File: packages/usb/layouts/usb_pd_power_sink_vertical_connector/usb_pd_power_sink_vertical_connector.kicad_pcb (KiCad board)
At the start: 2 copper layers, 8 parts, among them U2 2.9V

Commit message: WIP update usb
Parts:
- C1: value 1µF ±10% 16V X5R -> 1µF ±10% 25V X5R; footprint atopile:C0402-b3ef17 -> Samsung_Electro_Mechanics_CL05A105KA5NQNC:C0402
- R1, R2, R4: footprint atopile:R0402-56259e -> UNI_ROYAL_0402WGF1002TCE:R0402
- R3: footprint atopile:R0402-56259e -> UNI_ROYAL_0402WGF1001TCE:R0402
- U1: footprint atopile:ESSOP-10_L4.9-W3.9-P1.0-LS6.0-TL-EP-20a8ca -> WCH_CH224K:ESSOP-10_L4.9-W3.9-P1.0-LS6.0-TL-EP
- U2: footprint lib:LED0603-RD -> Hubei_KENTO_Elec_Blue_light_0603:LED0603-RD
- X1: footprint atopile:USB-C-TH_TYPE-C-USB-14P-1a34cb -> Jing_Extension_of_the_Electronic_Co_918_418K2022Y40000:USB-C-TH_TYPE-C-USB-14P
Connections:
- R2 pad 2: pd_trigger-line-1 -> pd_trigger-line
- R4 pad 1: pd_trigger-line -> pd_trigger-line-1
- U1 pad 2: pd_trigger.controller-line -> pd_trigger.controller-line-1
- U1 pad 3: pd_trigger.controller-line-1 -> pd_trigger.controller-line
- U1 pad 4: line -> line-1
- U1 pad 5: line-3 -> line
- U1 pad 6: line-1 -> line-2
- U1 pad 7: line-2 -> line-3
- U1 pad 8: pd_trigger-line-1 -> pd_trigger-line
- U1 pad 9: pd_trigger-line -> pd_trigger-line-1
- X1 pad 10: line-3 -> line
- X1 pad 11: line -> line-1
- X1 pad 12: line-2 -> line-3
- X1 pad 3: line-3 -> line
- X1 pad 4: line -> line-1
- X1 pad 5: line-1 -> line-2
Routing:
- net line-1: track 7.01 -> 10.6 mm, vias 1 -> 0
- net line: track 10.6 -> 7.72 mm
- net line-3: track 7.72 -> 7.02 mm, vias 0 -> 1

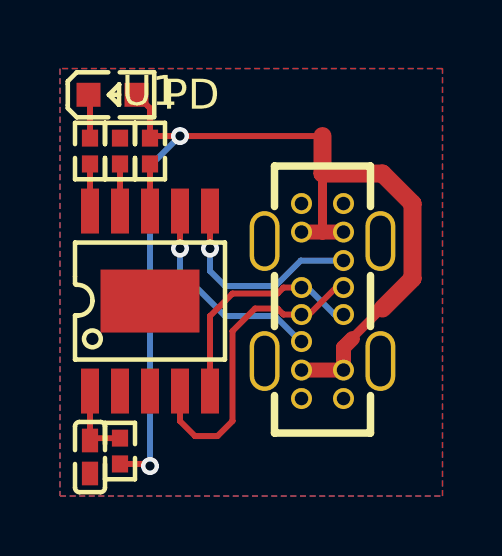
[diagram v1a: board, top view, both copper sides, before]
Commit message: Manually fix fp lib tables
fix some small bugs
fix package only modules (e.g. logos)
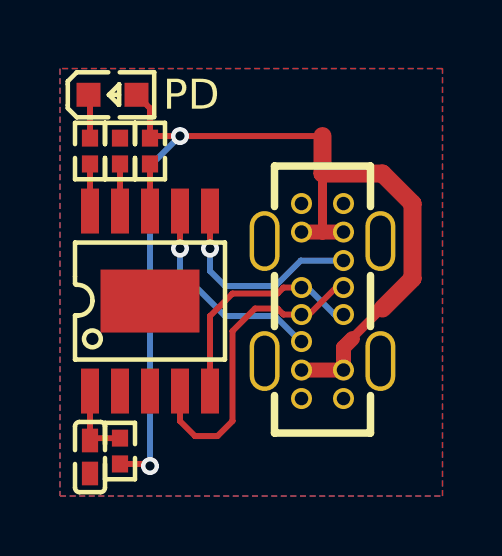
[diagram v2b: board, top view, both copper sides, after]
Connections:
- R2 pad 2: pd_trigger-line -> pd_trigger-line-1
- R4 pad 1: pd_trigger-line-1 -> pd_trigger-line
- U1 pad 4: line-1 -> line
- U1 pad 5: line -> line-2
- U1 pad 6: line-2 -> line-1
- U1 pad 8: pd_trigger-line -> pd_trigger-line-1
- U1 pad 9: pd_trigger-line-1 -> pd_trigger-line
- X1 pad 10: line -> line-2
- X1 pad 11: line-1 -> line
- X1 pad 3: line -> line-2
- X1 pad 4: line-1 -> line
- X1 pad 5: line-2 -> line-1
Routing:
- net line-1: track 10.6 -> 7.01 mm, vias 0 -> 1
- net line: track 7.72 -> 10.6 mm
- net line-2: track 7.01 -> 7.72 mm, vias 1 -> 0

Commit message: rebuild all packages & regenerate images of changed layouts (silk)
Add new scripts for version bump and build (based on atopile/packages)
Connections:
- U1 pad 2: pd_trigger.controller-line-1 -> pd_trigger.controller-line
- U1 pad 3: pd_trigger.controller-line -> pd_trigger.controller-line-1
- U1 pad 4: line -> line-3
- U1 pad 7: line-3 -> line
- X1 pad 11: line -> line-3
- X1 pad 12: line-3 -> line
- X1 pad 4: line -> line-3
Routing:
- net line-3: track 7.02 -> 10.6 mm, vias 1 -> 0
- net line: track 10.6 -> 7.02 mm, vias 0 -> 1
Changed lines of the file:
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@@
     )
     (net 0 "")
-    (net 1 "pd_trigger.controller-line")
-    (net 2 "pd_trigger.controller-line-1")
+    (net 1 "pd_trigger.controller-line-1")
+    (net 2 "pd_trigger.controller-line")
     (net 3 "pd_trigger-line-1")
     (net 4 "hv")
@@
     (net 7 "cathode")
     (net 8 "line-1")
-    (net 9 "line-3")
+    (net 9 "line")
     (net 10 "line-2")
-    (net 11 "line")
+    (net 11 "line-3")
     (net 12 "gnd")
     (net 13 "anode")
@@
             )
         )
-        (property "__atopile_lib_fp_hash__" "67c8cb14-7a56-5f37-cd49-de206344da21"
+        (property "__atopile_lib_fp_hash__" "316ee354-f06d-0bd8-88cd-489840625970"
             (at 0 0 0)
             (layer "User.9")
@@
             )
         )
-        (property "checksum" "92e079f9d1334f588ddb127873738a56bad1b8f57794e6d8826a1dbb9b5fecef"
+        (property "checksum" "84749ec1cd5fbb3976a4ef85d04dc245f71ce15cbd4539127e07cf8da310f7ce"
             (at 0 0 0)
             (layer "User.9")
@@
             (size 1.5 0.6)
             (layers "F.Cu" "F.Mask" "F.Paste")
-            (net 2 "pd_trigger.controller-line-1")
+            (net 2 "pd_trigger.controller-line")
         )
         (pad "3" smd rect
@@
             (size 1.5 0.6)
             (layers "F.Cu" "F.Mask" "F.Paste")
-            (net 1 "pd_trigger.controller-line")
+            (net 1 "pd_trigger.controller-line-1")
         )
         (pad "4" smd rect
@@
             (size 1.5 0.6)
             (layers "F.Cu" "F.Mask" "F.Paste")
-            (net 11 "line")
+            (net 11 "line-3")
         )
         (pad "5" smd rect
@@
             (size 1.5 0.6)
             (layers "F.Cu" "F.Mask" "F.Paste")
-            (net 9 "line-3")
+            (net 9 "line")
         )
         (pad "8" smd rect
@@
             (drill 0.4499864)
             (layers "*.Cu" "*.Mask")
-            (net 11 "line")
+            (net 11 "line-3")
         )
         (pad "5" thru_hole circle
@@
             (drill 0.4499864)
             (layers "*.Cu" "*.Mask")
-            (net 11 "line")
+            (net 11 "line-3")
         )
         (pad "12" thru_hole circle
@@
             (drill 0.4499864)
             (layers "*.Cu" "*.Mask")
-            (net 9 "line-3")
+            (net 9 "line")
         )
         (pad "13" thru_hole circle

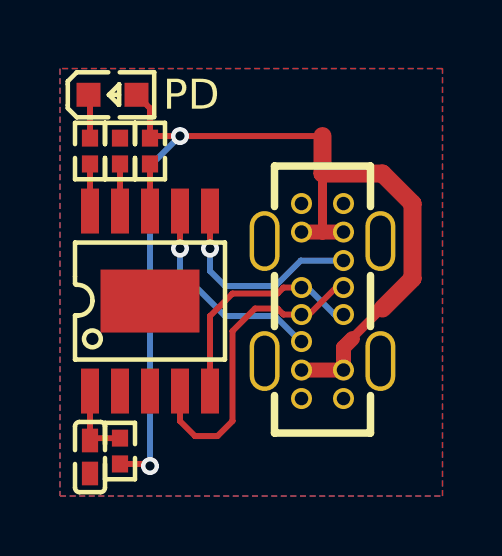
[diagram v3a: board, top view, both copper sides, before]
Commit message: Use packages from packages folder
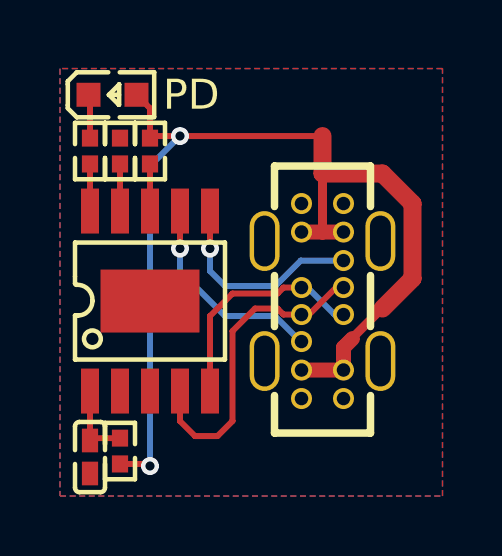
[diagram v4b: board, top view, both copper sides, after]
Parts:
- removed U2: 2.9V, Hubei_KENTO_Elec_Blue_light_0603:LED0603-RD
- added LED1: , Hubei_KENTO_Elec_Blue_light_0603:LED0603-RD, F.Cu at (-7.00, -6.88)
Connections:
- net line-2 renamed Dneg
- net line-3 renamed Dpos
